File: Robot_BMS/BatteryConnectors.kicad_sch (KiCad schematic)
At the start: 3 parts

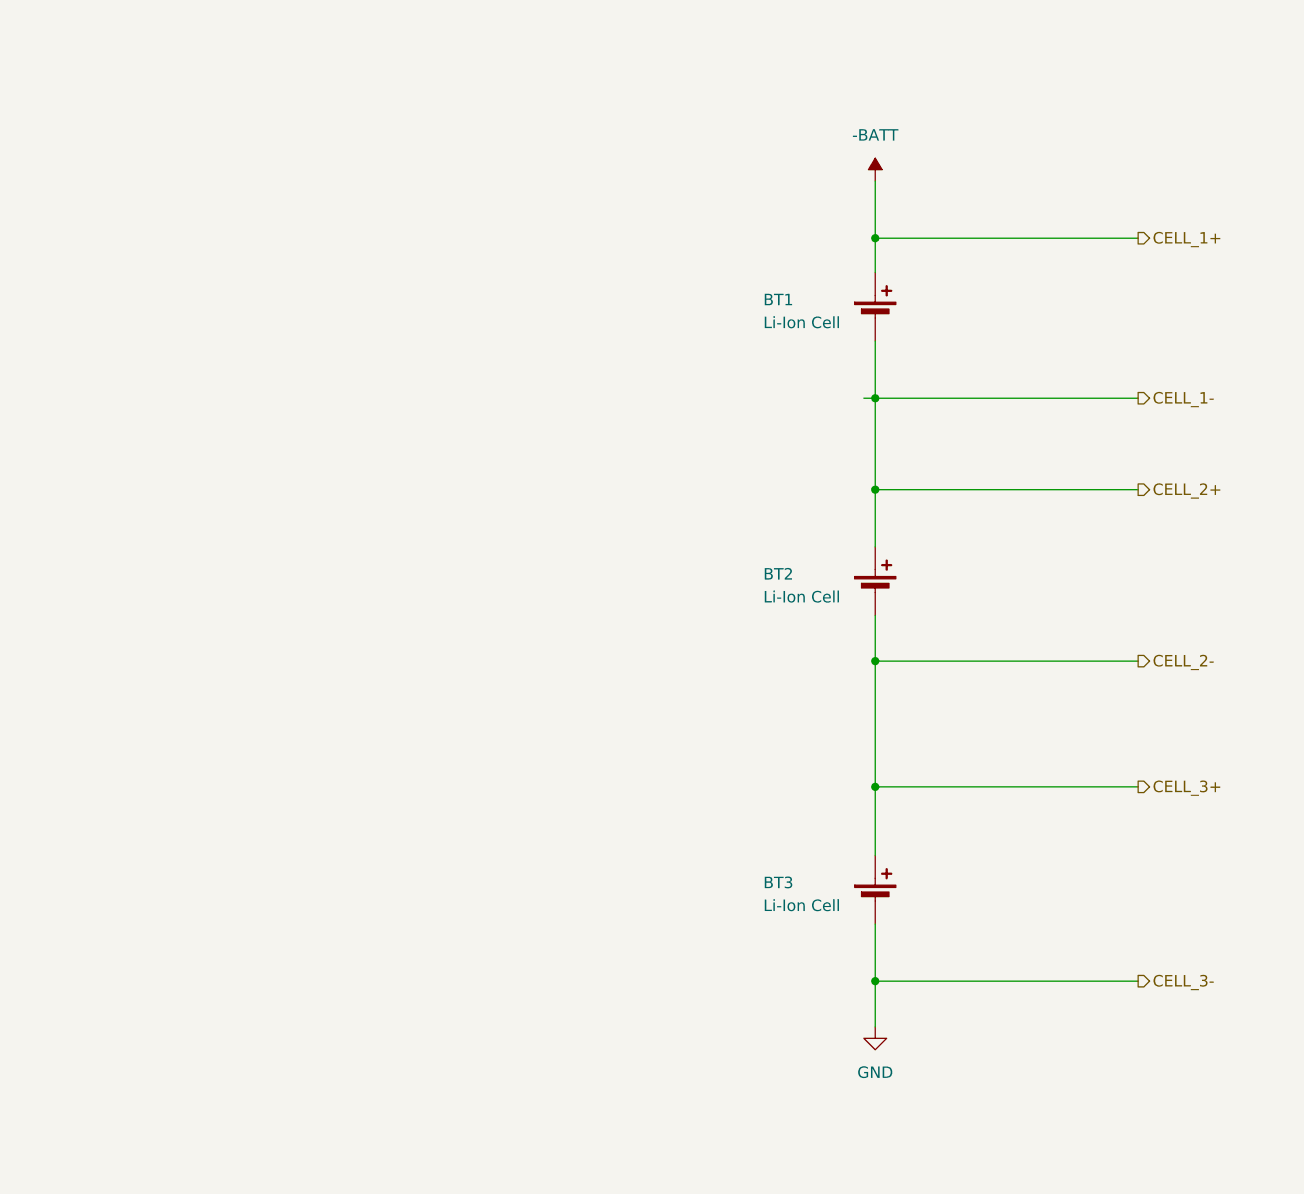
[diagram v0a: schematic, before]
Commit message: DC power supply added via dc Barrel jack
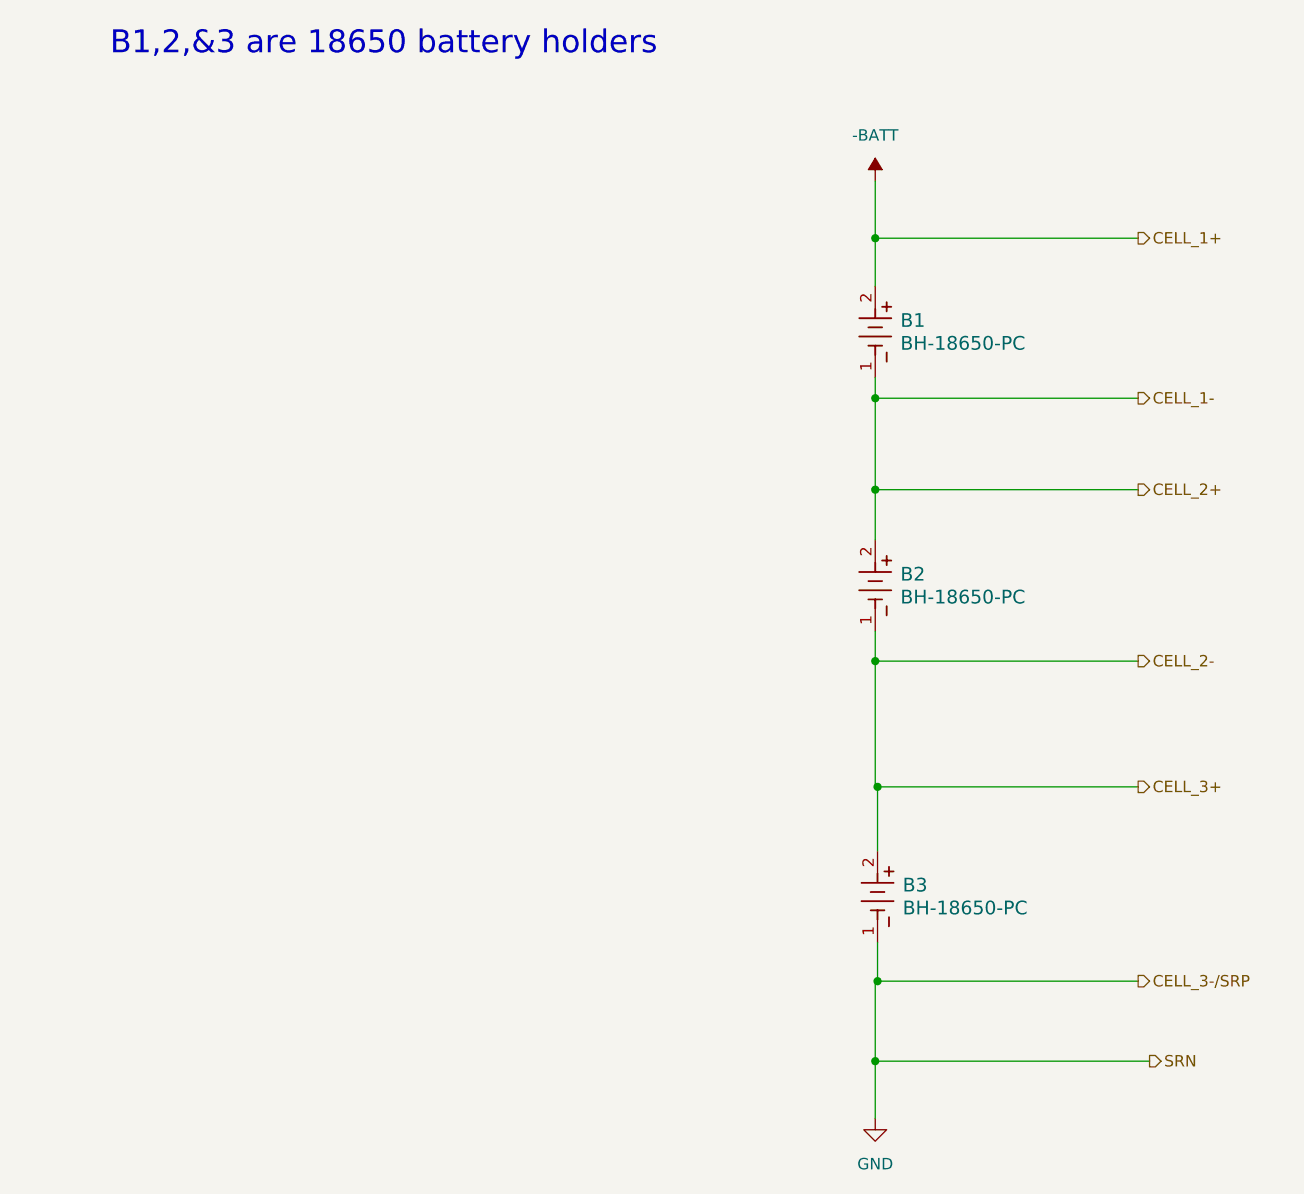
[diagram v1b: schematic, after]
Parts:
- removed BT1, BT2, BT3: Li-Ion Cell, symbol Device:Battery_Cell
- added B1, B2, B3: BH-18650-PC, BAT_BH-18650-PC_MPD, symbol 18650 Battery Holder:BH-18650-PC
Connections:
- net -BATT: now also B1.2
- net CELL_1-: now also B1.1, B2.2
- net CELL_2-: now also B2.1, B3.2
- net GND: now also B3.1
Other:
- note added: "B1,2,&3 are 18650 battery holders"

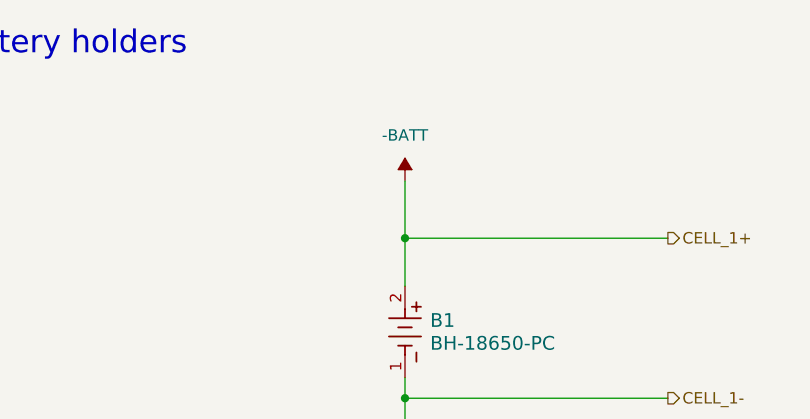
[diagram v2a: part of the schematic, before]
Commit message: solar charger set to 15V
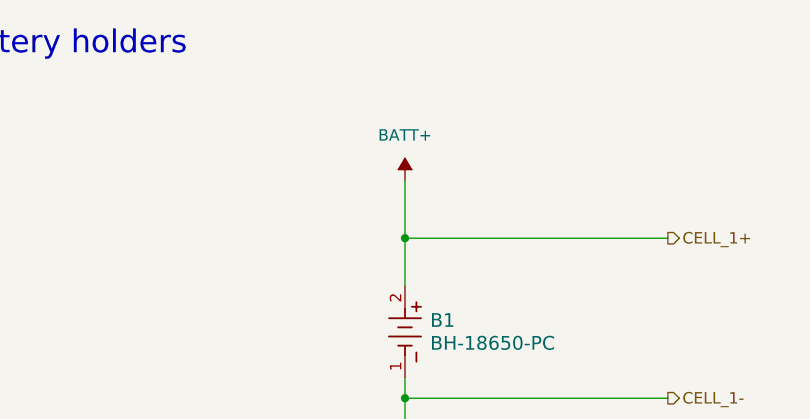
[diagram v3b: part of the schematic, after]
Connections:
- net -BATT renamed BATT+
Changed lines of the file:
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@@
 		(dnp no)
 		(fields_autoplaced yes)
-		(property "Reference" "#PWR018"
+		(property "Reference" "#PWR023"
 			(at 114.3 55.88 0)
 			(effects
@@
 			)
 		)
-		(property "Value" "-BATT"
+		(property "Value" "BATT+"
 			(at 114.3 46.99 0)
 			(effects
@@
 			(project "Robot_BMS"
 				(path "/72551b1c-3d40-4199-8911-e5b015f4abec/e8cba041-cae9-4c3d-bb1a-67e8763cb5b9"
-					(reference "#PWR018")
+					(reference "#PWR023")
 					(unit 1)
 				)
@@
 		(dnp no)
 		(fields_autoplaced yes)
-		(property "Reference" "#PWR019"
+		(property "Reference" "#PWR024"
 			(at 114.3 162.56 0)
 			(effects
@@
 			(project "Robot_BMS"
 				(path "/72551b1c-3d40-4199-8911-e5b015f4abec/e8cba041-cae9-4c3d-bb1a-67e8763cb5b9"
-					(reference "#PWR019")
+					(reference "#PWR024")
 					(unit 1)
 				)
